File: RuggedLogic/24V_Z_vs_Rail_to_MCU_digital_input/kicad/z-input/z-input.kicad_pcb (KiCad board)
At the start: 2 copper layers, 80 x 48.3 mm, 17 parts, among them J1 Sensor, J2 24V, J3 3V3_OUT, J4 Select, T1 BCP5616Q, U1 APC-817B-SL, U2 OPB616

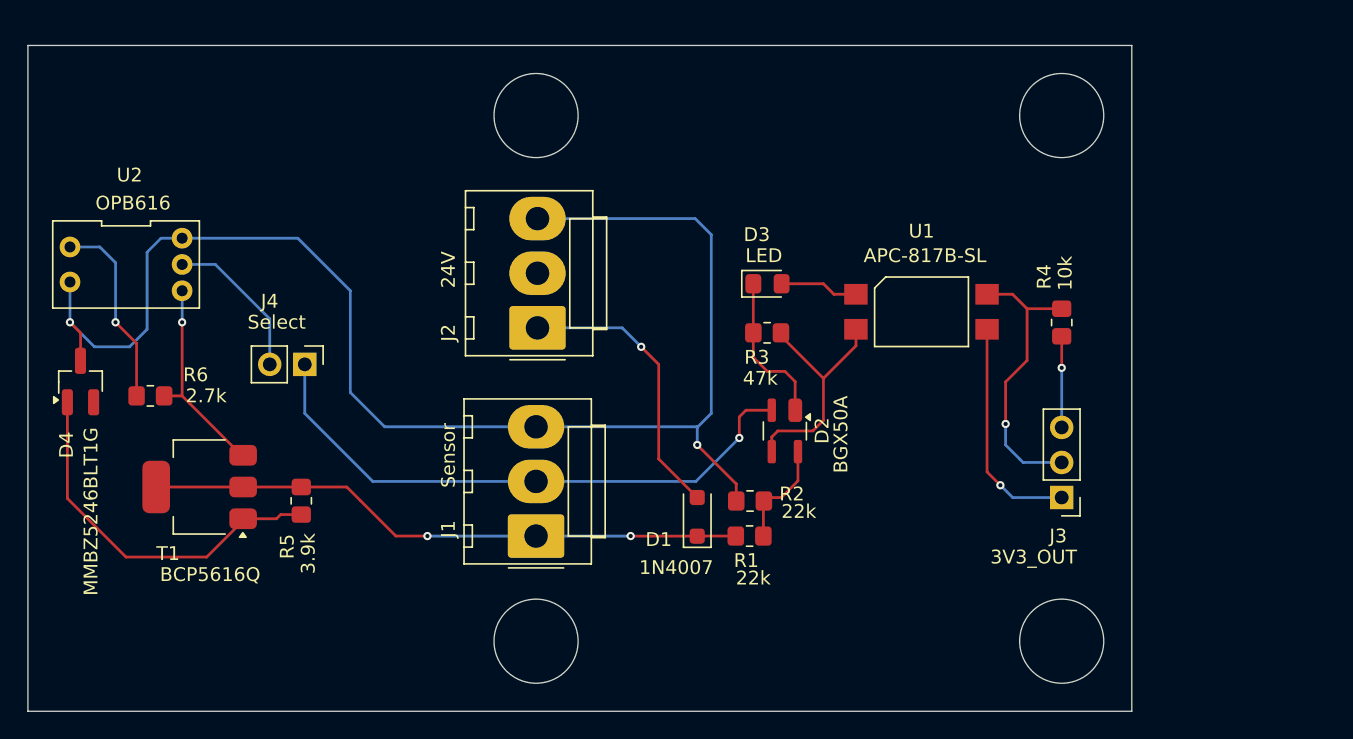
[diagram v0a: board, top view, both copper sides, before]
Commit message: Redone Z-input PCB; production update
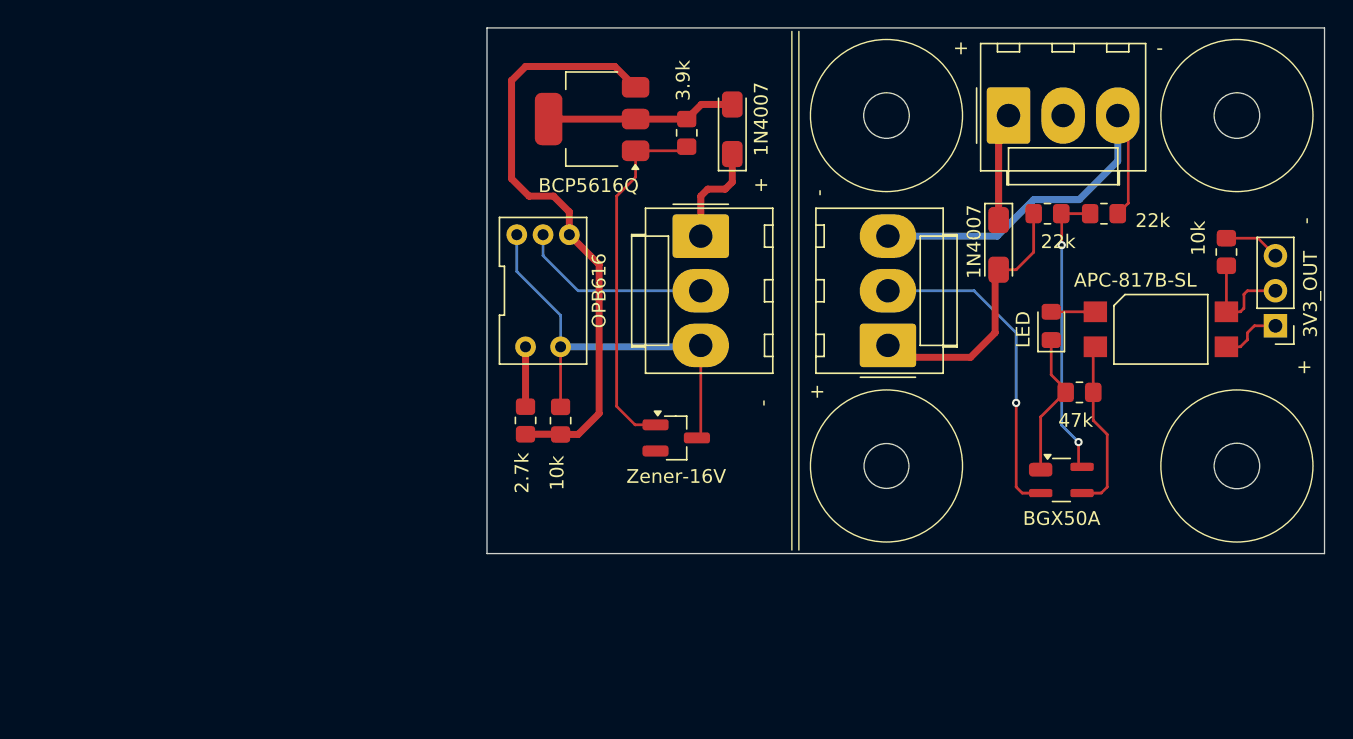
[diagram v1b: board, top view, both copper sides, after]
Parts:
- removed J4: Select, Connector_PinHeader_2.54mm:PinHeader_1x02_P2.54mm_Vertical
- added D5: 1N4007, Secoh:D_SOD-123F_hand_soldering, F.Cu at (115.8, 51.8)
- added J1_B1: 24V_SNS, Connector_Molex:Molex_KK-396_A-41791-0003_1x03_P3.96mm_Vertical, F.Cu at (113.5, 59.5)
- added R7: 10k, Resistor_SMD:R_0805_2012Metric_Pad1.20x1.40mm_HandSolder, F.Cu at (103.4, 72.9)
- D1: footprint Secoh:D_SOD-123F_inverted_polarity -> Secoh:D_SOD-123F_hand_soldering
- D4: value MMBZ5246BLT1G -> Zener-16V
- J1: value Sensor -> 24V_SNS
- moved D4 43.4 mm to (111.8, 74.2), turned to 0 degrees
- moved T1 39.0 mm to (105.7, 51.1)
- moved R5 38.6 mm to (112.5, 52.1)
- moved J2 37.4 mm to (135.8, 50.8), turned to 0 degrees
- moved R2 33.0 mm to (142.8, 57.9), turned to 0 degrees
- moved R1 31.8 mm to (138.7, 57.9)
- moved U2 30.3 mm to (102.1, 63.5), turned to 0 degrees
- moved D1 29.4 mm to (135.1, 60.2), turned to -90 degrees
- moved J1 29.0 mm to (127.1, 67.5)
- moved R6 27.3 mm to (100.8, 72.9), turned to 90 degrees
- moved R3 23.0 mm to (141.0, 70.9)
- moved D3 20.8 mm to (138.9, 66.0), turned to 90 degrees
- moved D2 20.4 mm to (139.7, 77.2), turned to 0 degrees
- moved J3 19.9 mm to (155.2, 66.0)
- moved U1 17.4 mm to (146.9, 66.3)
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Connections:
- J1 pad 3: Net-(D4-E) -> Net-(J1-Pin_3)
- J2 pad 3: Net-(D4-E) -> Net-(J1-Pin_3)
- R2 pad 2: Net-(D4-E) -> Net-(J1-Pin_3)
- R5 pad 1: Net-(D1--) -> Net-(D5--)
- T1 pad 2: Net-(D1--) -> Net-(D5--)
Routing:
- net Net-(D4-E): track 102.7 -> 30.8 mm, vias 2 -> 0
- net Net-(J1-Pin_3): track 0.00 -> 30.0 mm
- net Net-(T1-E): track 15.1 -> 43.8 mm, vias 1 -> 0
- net Net-(D1--): track 43.5 -> 19.6 mm, vias 2 -> 0
- net Net-(J1-Pin_2): track 42.5 -> 23.7 mm
- net Net-(D5--): track 0.00 -> 13.7 mm
- net Net-(D2-Pad4): track 7.75 -> 21.0 mm, vias 0 -> 2
- net Net-(J3-Pin_2): track 21.0 -> 8.12 mm, vias 1 -> 0
- net Net-(D1-+): track 20.7 -> 8.13 mm, vias 1 -> 0
- net Net-(J3-Pin_1): track 16.5 -> 4.48 mm, vias 1 -> 0
- net Net-(U2-Pin_1): track 14.1 -> 4.33 mm, vias 1 -> 0
- net Net-(D5-+): track 0.00 -> 7.64 mm
- net Net-(D2--): track 17.5 -> 12.7 mm
- net Net-(J1_B1-Pin_2): track 11.3 -> 14.0 mm
- net Net-(J3-Pin_3): track 6.60 -> 4.08 mm, vias 1 -> 0
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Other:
- board size 80 x 48.3 mm -> 60.7 x 38.1 mm
- board text added: "+"
- board text added: "-"

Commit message: Fixed errors in Rugged Z sensor Fixes to Rugged Switch
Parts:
- D3: footprint LED_SMD:LED_0805_2012Metric_Pad1.15x1.40mm_HandSolder -> Secoh:LED_0805
- D4: value Zener-16V -> Zener-16V-SOT23
- R5: value 3.9k -> 3.3k
- R6: value 2.7k -> 2.2k
- moved R4 7.66 mm to (152.7, 68.3), turned to 0 degrees
- moved J3 6.29 mm to (155.0, 59.8), turned to 0 degrees
- moved U1 2.03 mm to (146.9, 64.3)
- moved D4 1.13 mm to (112.5, 73.3), turned to -90 degrees
- turned D5 to -90 degrees
- turned D1 to 90 degrees
- turned D3 to -90 degrees
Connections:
- D1 pad 1: Net-(D1-+) -> Net-(D1-K)
- D1 pad 2: Net-(D1--) -> Net-(D1-A)
- D3 pad 1: Net-(D2-+) -> Net-(D3-K)
- D3 pad 2: Net-(D3--) -> Net-(D2-+)
- D4 pad 1: Net-(D4-B) -> Net-(D4-A)
- D4 pad 3: Net-(D4-E) -> Net-(D4-K)
- D5 pad 1: Net-(D5-+) -> Net-(D5-K)
- D5 pad 2: Net-(D5--) -> Net-(D5-A)
- J1 pad 1: Net-(D1--) -> Net-(D1-K)
- J1_B1 pad 1: Net-(D5-+) -> Net-(D5-A)
- J1_B1 pad 3: Net-(D4-E) -> Net-(D4-A)
- J2 pad 1: Net-(D1-+) -> Net-(D1-A)
- R1 pad 1: Net-(D1--) -> Net-(D1-K)
- R5 pad 1: Net-(D5--) -> Net-(D5-K)
- R5 pad 2: Net-(D4-B) -> Net-(D4-K)
- R7 pad 2: Net-(D4-E) -> Net-(D4-A)
- T1 pad 1: Net-(D4-B) -> Net-(D4-K)
- T1 pad 2: Net-(D5--) -> Net-(D5-K)
- U1 pad 1: Net-(D3--) -> Net-(D3-K)
- U1 pad 3: Net-(J3-Pin_1) -> Net-(J3-Pin_2)
- U1 pad 4: Net-(J3-Pin_2) -> Net-(J3-Pin_1)
- U2 pad 2: Net-(D4-E) -> Net-(D4-A)
- U2 pad 5: Net-(D4-E) -> Net-(D4-A)
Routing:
- net Net-(D4-E): track 30.8 -> 0.00 mm
- net Net-(D4-K): track 0.00 -> 29.4 mm
- net Net-(D4-A): track 0.00 -> 28.0 mm
- net Net-(D4-B): track 26.3 -> 0.00 mm
- net Net-(D1-K): track 0.00 -> 19.6 mm
- net Net-(D1--): track 19.6 -> 0.00 mm
- net Net-(D5-K): track 0.00 -> 13.7 mm
- net Net-(D5--): track 13.7 -> 0.00 mm
- net Net-(D1-A): track 0.00 -> 8.13 mm
- net Net-(D1-+): track 8.13 -> 0.00 mm
- net Net-(D5-A): track 0.00 -> 7.64 mm
- net Net-(D5-+): track 7.64 -> 0.00 mm
- net Net-(D3-K): track 0.00 -> 4.86 mm
- net Net-(D3--): track 3.20 -> 0.00 mm
- net Net-(D2--): track 12.7 -> 14.7 mm
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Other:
- board text added: "out"
